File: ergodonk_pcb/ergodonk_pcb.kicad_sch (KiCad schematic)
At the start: 117 parts, among them J1 AudioJack4, Q1 TIP120, U1 Solenoid

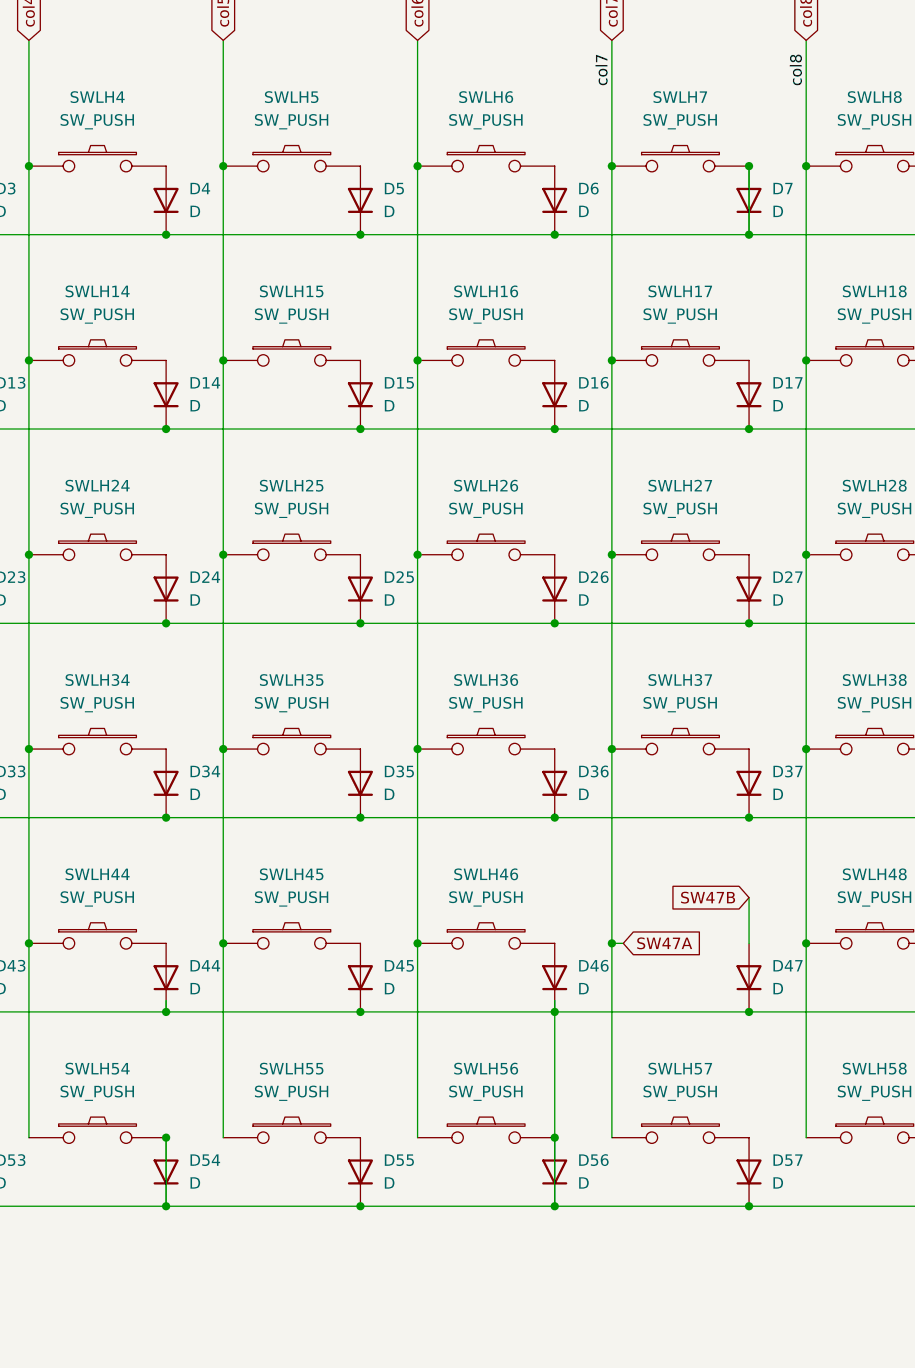
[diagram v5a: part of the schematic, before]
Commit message: Updated wiring on pcb to v2, ran DRC
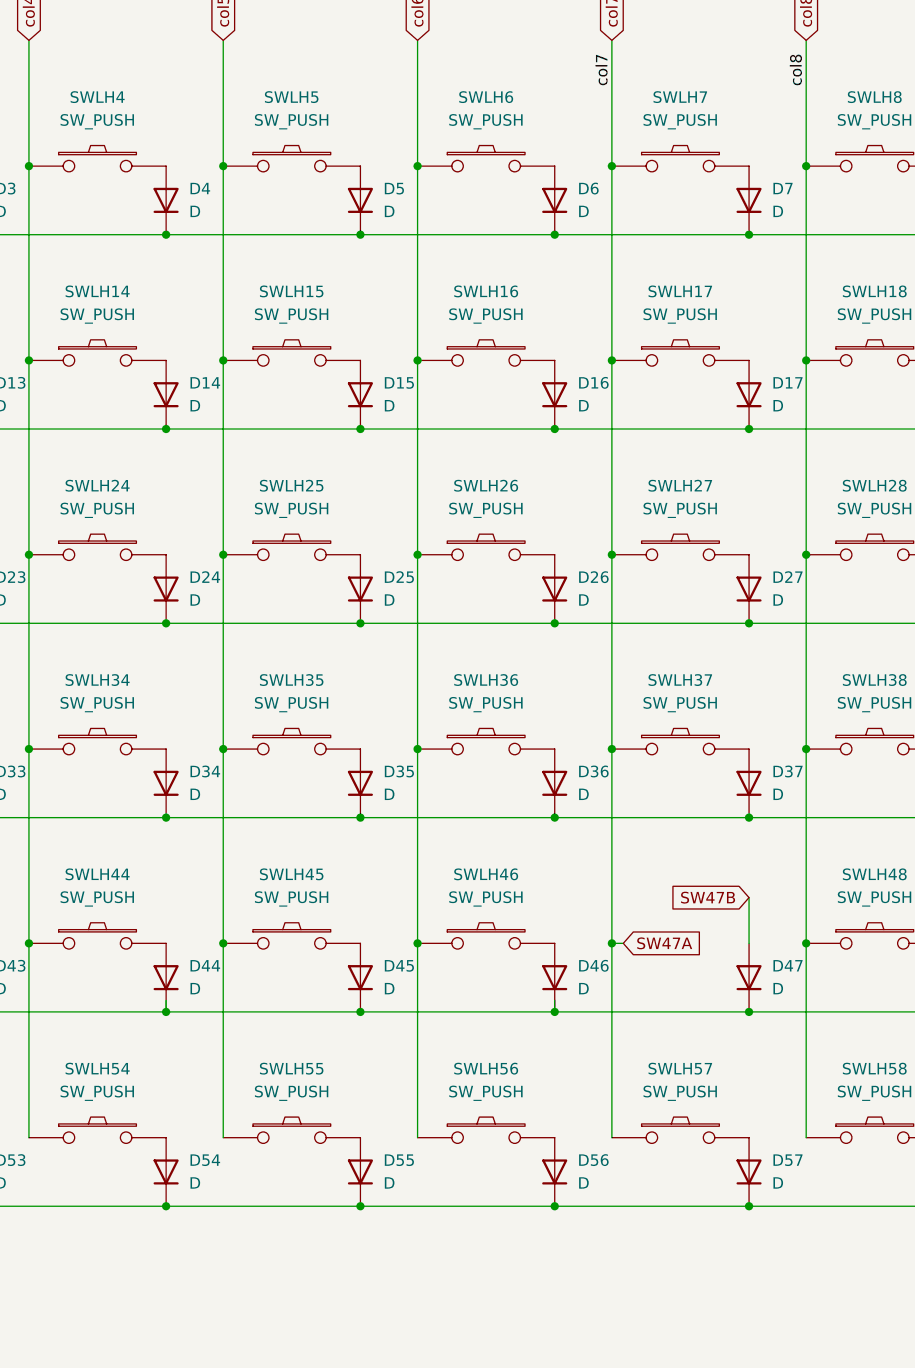
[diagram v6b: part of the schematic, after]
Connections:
- net row0: no longer D7.2 (A), SWLH7.2
- net row4: no longer D50.1 (K), D51.1 (K), D52.1 (K), D53.1 (K), D54.1 (K), D54.2 (A), D55.1 (K), D56.1 (K), D56.2 (A), D57.1 (K), D58.1 (K), SWLH54.2, SWLH56.2, ULH1.10 (PA15)
- new net: D56.2 (A), SWLH56.2
- new net: D7.2 (A), SWLH7.2
- new net: D54.2 (A), SWLH54.2
- new net row5: D50.1 (K), D51.1 (K), D52.1 (K), D53.1 (K), D54.1 (K), D55.1 (K), D56.1 (K), D57.1 (K), D58.1 (K), ULH1.10 (PA15)
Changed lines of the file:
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@@
   (junction (at 364.49 88.9) (diameter 0) (color 0 0 0 0)
   )
-  (junction (at 379.73 45.72) (diameter 0) (color 0 0 0 0)
-  )
   (junction (at 201.93 44.45) (diameter 0) (color 0 0 0 0)
   )
@@
   (junction (at 299.72 88.9) (diameter 0) (color 0 0 0 0)
   )
-  (junction (at 314.96 153.67) (diameter 0) (color 0 0 0 0)
-  )
   (junction (at 250.19 118.11) (diameter 0) (color 0 0 0 0)
   )
@@
   )
   (junction (at 271.78 53.34) (diameter 0) (color 0 0 0 0)
-  )
-  (junction (at 358.14 153.67) (diameter 0) (color 0 0 0 0)
   )
   (junction (at 379.73 139.7) (diameter 0) (color 0 0 0 0)
@@
     (stroke (width 0) (type default) (color 0 0 0 0))
   )
-  (wire (pts (xy 314.96 153.67) (xy 314.96 161.29))
-    (stroke (width 0) (type default) (color 0 0 0 0))
-  )
   (wire (pts (xy 228.6 139.7) (xy 250.19 139.7))
     (stroke (width 0) (type default) (color 0 0 0 0))
@@
     (stroke (width 0) (type default) (color 0 0 0 0))
   )
-  (wire (pts (xy 358.14 139.7) (xy 358.14 153.67))
-    (stroke (width 0) (type default) (color 0 0 0 0))
-  )
   (wire (pts (xy 234.95 132.08) (xy 234.95 153.67))
     (stroke (width 0) (type default) (color 0 0 0 0))
@@
     (stroke (width 0) (type default) (color 0 0 0 0))
   )
-  (wire (pts (xy 358.14 153.67) (xy 358.14 161.29))
-    (stroke (width 0) (type default) (color 0 0 0 0))
-  )
   (wire (pts (xy 116.84 33.02) (xy 143.51 33.02))
     (stroke (width 0) (type default) (color 0 0 0 0))
@@
     (stroke (width 0) (type default) (color 0 0 0 0))
   )
-  (wire (pts (xy 379.73 45.72) (xy 379.73 53.34))
-    (stroke (width 0) (type default) (color 0 0 0 0))
-  )

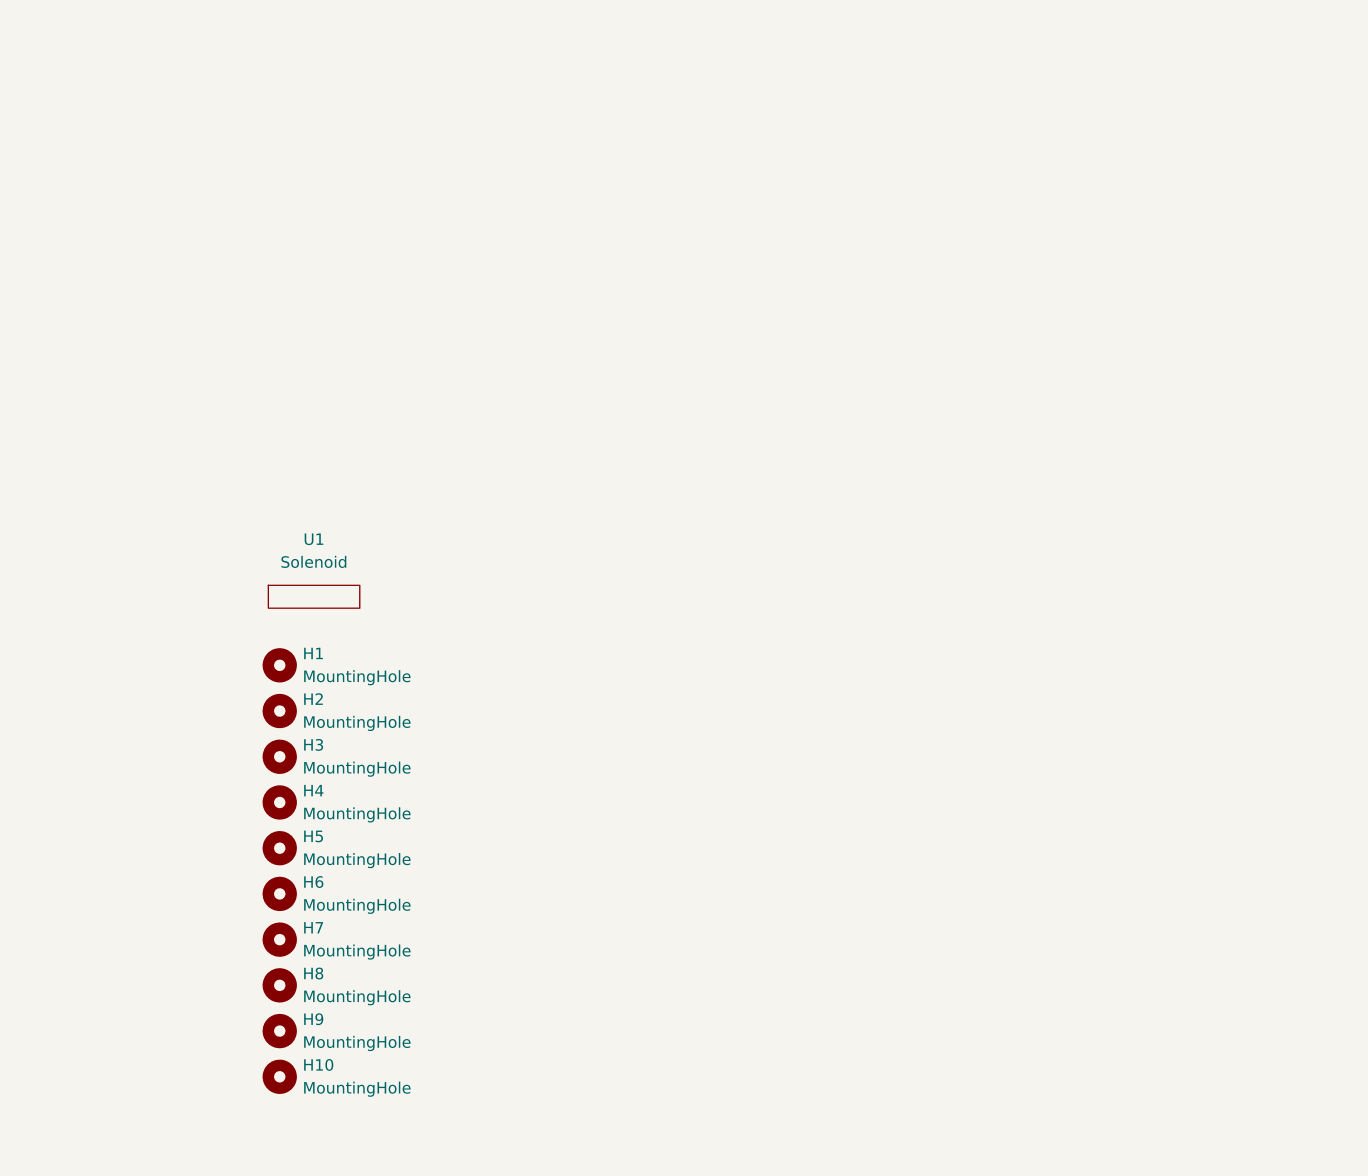
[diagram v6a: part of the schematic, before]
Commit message: Added KiCad libraries for rp2040 pro micro and Sofle Choc
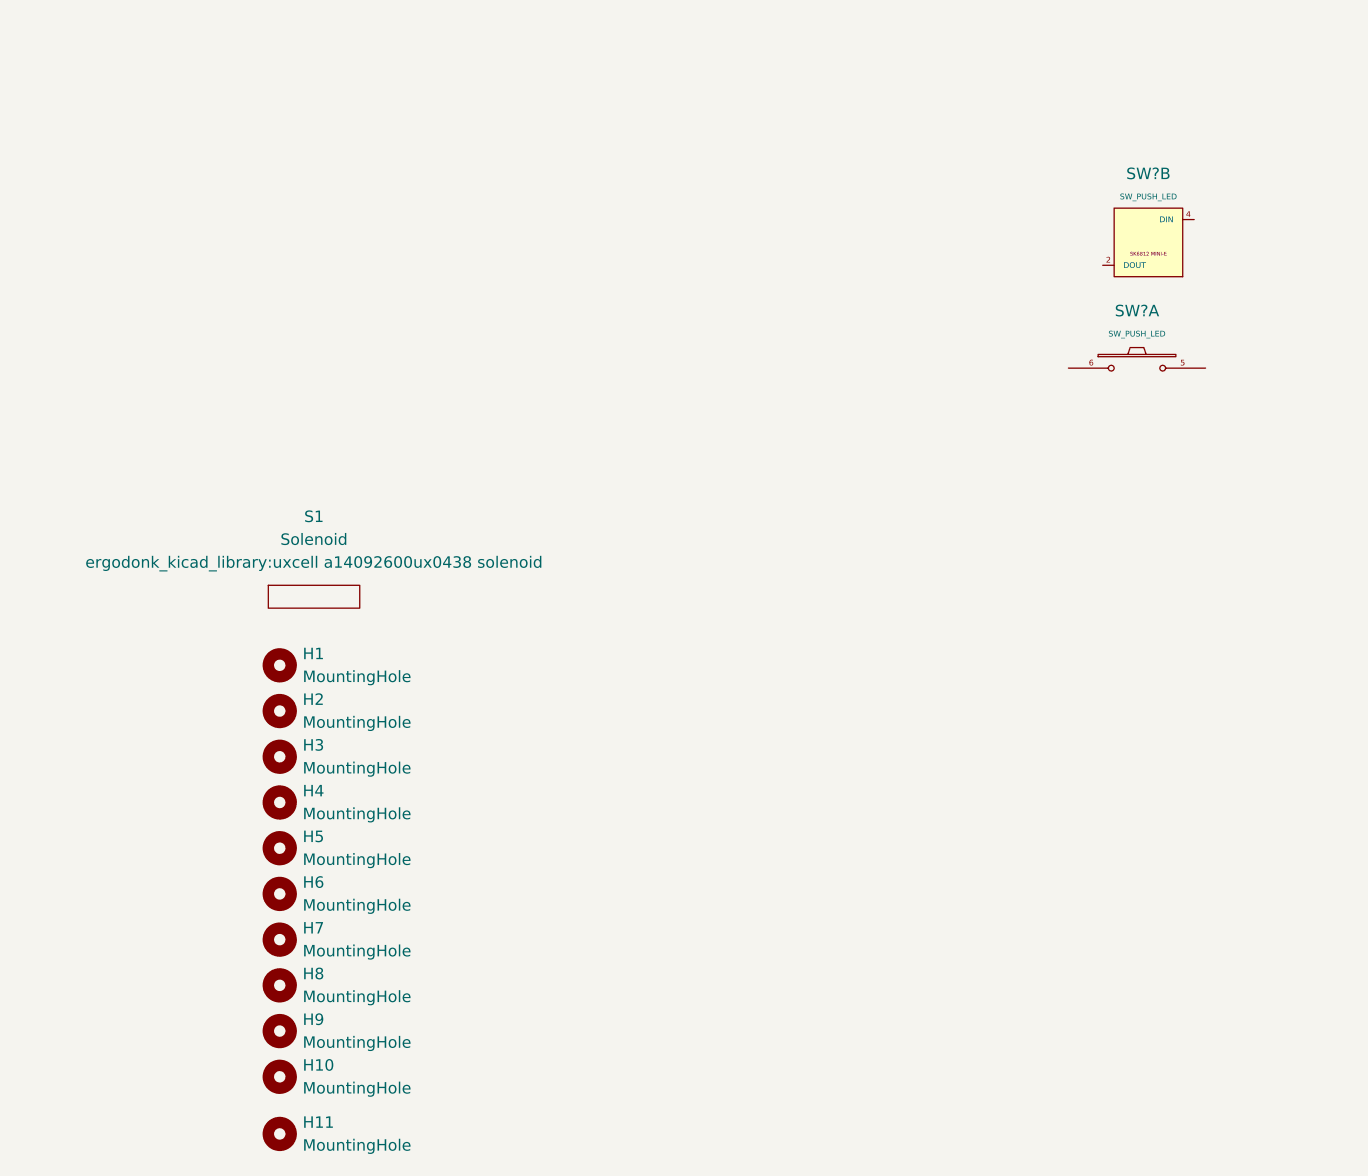
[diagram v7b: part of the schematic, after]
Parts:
- added H11: MountingHole, MountingHole:MountingHole_2.2mm_M2_Pad_Via, symbol Mechanical:MountingHole
- added SW? (x2): SW_PUSH_LED, SofleRGB:Choc_Hotswap_SK6812MiniE, symbol SofleKeyboard:SW_PUSH_LED
- renumbered U1 to S1
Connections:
- net GND: now also SW?.3 (GND)
- new net VDD: SW?.1 (VDD)
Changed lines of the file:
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@@
     (pin "3")
+  )
+  (symbol (lib_id "Mechanical:MountingHole") (at 20.32 264.16 0) (unit 1)
+    (in_bom yes) (on_board yes) (fields_autoplaced)
+    (property "Reference" "H11" (id 0) (at 22.86 262.8899 0)
+      (effects (font (size 1.27 1.27)) (justify left))
+    )
+    (property "Value" "MountingHole" (id 1) (at 22.86 265.4299 0)
+      (effects (font (size 1.27 1.27)) (justify left))
+    )
+    (property "Footprint" "MountingHole:MountingHole_2.2mm_M2_Pad_Via" (id 2) (at 20.32 264.16 0)
+      (effects (font (size 1.27 1.27)) hide)
+    )
+    (property "Datasheet" "~" (id 3) (at 20.32 264.16 0)
+      (effects (font (size 1.27 1.27)) hide)
+    )
   )
   (symbol (lib_id "kbd:SW_PUSH") (at 393.7 132.08 0) (unit 1)
@@
     (pin "2")
   )
+  (symbol (lib_id "SofleKeyboard:SW_PUSH_LED") (at 116.84 165.1 0) (unit 2)
+    (in_bom yes) (on_board yes) (fields_autoplaced)
+    (property "Reference" "SW?" (id 0) (at 116.84 157.48 0))
+    (property "Value" "SW_PUSH_LED" (id 1) (at 116.84 160.02 0)
+      (effects (font (size 0.635 0.635)))
+    )
+    (property "Footprint" "SofleRGB:Choc_Hotswap_SK6812MiniE" (id 2) (at 117.602 160.02 0)
+      (effects (font (size 1.27 1.27)) hide)
+    )
+    (property "Datasheet" "" (id 3) (at 116.84 162.56 0)
+      (effects (font (size 1.27 1.27)) hide)
+    )
+    (pin "5")
+    (pin "6")
+    (pin "1")
+    (pin "2")
+    (pin "3")
+    (pin "4")
+  )
   (symbol (lib_id "MUR340S:MUR340S") (at 201.93 29.21 90) (unit 1)
     (in_bom yes) (on_board yes) (fields_autoplaced)
@@
     (pin "2")
   )
+  (symbol (lib_id "SofleKeyboard:SW_PUSH_LED") (at 115.57 179.07 0) (unit 1)
+    (in_bom yes) (on_board yes) (fields_autoplaced)
+    (property "Reference" "SW?" (id 0) (at 115.57 172.72 0))
+    (property "Value" "SW_PUSH_LED" (id 1) (at 115.57 175.26 0)
+      (effects (font (size 0.635 0.635)))
+    )
+    (property "Footprint" "SofleRGB:Choc_Hotswap_SK6812MiniE" (id 2) (at 116.332 173.99 0)
+      (effects (font (size 1.27 1.27)) hide)
+    )
+    (property "Datasheet" "" (id 3) (at 115.57 176.53 0)
+      (effects (font (size 1.27 1.27)) hide)
+    )
+    (pin "5")
+    (pin "6")
+    (pin "1")
+    (pin "2")
+    (pin "3")
+    (pin "4")
+  )
   (symbol (lib_id "kbd:SW_PUSH") (at 264.16 153.67 0) (unit 1)
     (in_bom yes) (on_board yes) (fields_autoplaced)
@@
   (symbol (lib_id "Neff_KiCad_Symbol_library:Solenoid") (at 24.13 204.47 0) (unit 1)
     (in_bom yes) (on_board yes) (fields_autoplaced)
-    (property "Reference" "U1" (id 0) (at 24.13 198.12 0))
-    (property "Value" "Solenoid" (id 1) (at 24.13 200.66 0))
-    (property "Footprint" "ergodonk_kicad_library:uxcell a14092600ux0438 solenoid" (id 2) (at 24.13 204.47 0)
-      (effects (font (size 1.27 1.27)) hide)
-    )
+    (property "Reference" "S1" (id 0) (at 24.13 195.58 0))
+    (property "Value" "Solenoid" (id 1) (at 24.13 198.12 0))
+    (property "Footprint" "ergodonk_kicad_library:uxcell a14092600ux0438 solenoid" (id 2) (at 24.13 200.66 0))
     (property "Datasheet" "" (id 3) (at 24.13 204.47 0)
       (effects (font (size 1.27 1.27)) hide)
@@
       (reference "H10") (unit 1) (value "MountingHole") (footprint "MountingHole:MountingHole_2.2mm_M2_Pad_Via")
     )
+    (path "/281f3b35-c9c9-4da9-a161-2cabb2abf79f"
+      (reference "H11") (unit 1) (value "MountingHole") (footprint "MountingHole:MountingHole_2.2mm_M2_Pad_Via")
+    )
     (path "/099c249e-19b1-420b-ac1a-d5f68deca6eb"
       (reference "J1") (unit 1) (value "AudioJack4") (footprint "kbd:MJ-4PP-9")
@@
       (reference "R2") (unit 1) (value "1k") (footprint "Resistor_THT:R_Axial_DIN0207_L6.3mm_D2.5mm_P10.16mm_Horizontal")
     )
+    (path "/a911a847-2802-4dd4-b6d0-33573b4d1ba3"
+      (reference "S1") (unit 1) (value "Solenoid") (footprint "ergodonk_kicad_library:uxcell a14092600ux0438 solenoid")
+    )
+    (path "/6ec1bd7a-4a4d-4118-9cd2-ebbe2cd7b66d"
+      (reference "SW?") (unit 1) (value "SW_PUSH_LED") (footprint "SofleRGB:Choc_Hotswap_SK6812MiniE")
+    )
+    (path "/410c5709-5919-455c-bdd2-37c964eec349"
+      (reference "SW?") (unit 2) (value "SW_PUSH_LED") (footprint "SofleRGB:Choc_Hotswap_SK6812MiniE")
+    )
     (path "/adfb317f-8711-4175-930d-37a9aacb659b"
       (reference "SWLH1") (unit 1) (value "SW_PUSH") (footprint "ergodonk_kicad_library:CherryMX_Hotswap")
@@
       (reference "SWLH_ROT1") (unit 1) (value "RotaryEncoder_Switch") (footprint "ergodonk_kicad_library:RotaryEncoder_EC11_with_MX_hotswap_v2")
     )
-    (path "/a911a847-2802-4dd4-b6d0-33573b4d1ba3"
-      (reference "U1") (unit 1) (value "Solenoid") (footprint "ergodonk_kicad_library:uxcell a14092600ux0438 solenoid")
-    )
     (path "/c103fff7-a3eb-4bac-9615-edfd2f702179"
